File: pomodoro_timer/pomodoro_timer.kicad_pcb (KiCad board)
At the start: 2 copper layers, 68.1 x 78.1 mm, 37 parts, among them J1 UPDI Flash Header, J2 I2C Header, P1 Conn_USB_A_Plain, Q1 MOSFET SOT23, SW1 Start/Stop, SW2 Skip, SW3 Restart, U1 ATtiny412, U10 WS2812B, U11 WS2812B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

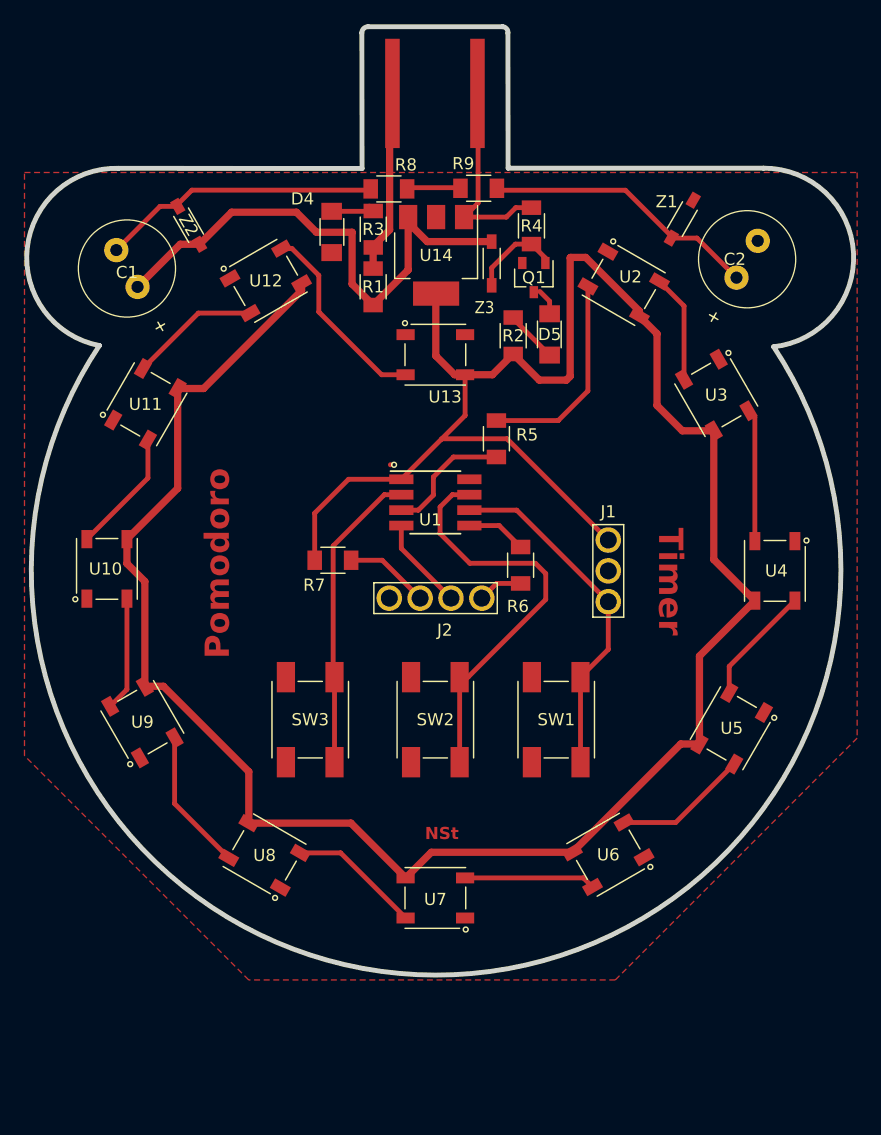
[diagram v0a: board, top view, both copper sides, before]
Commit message: PCB: updated schematics and routing
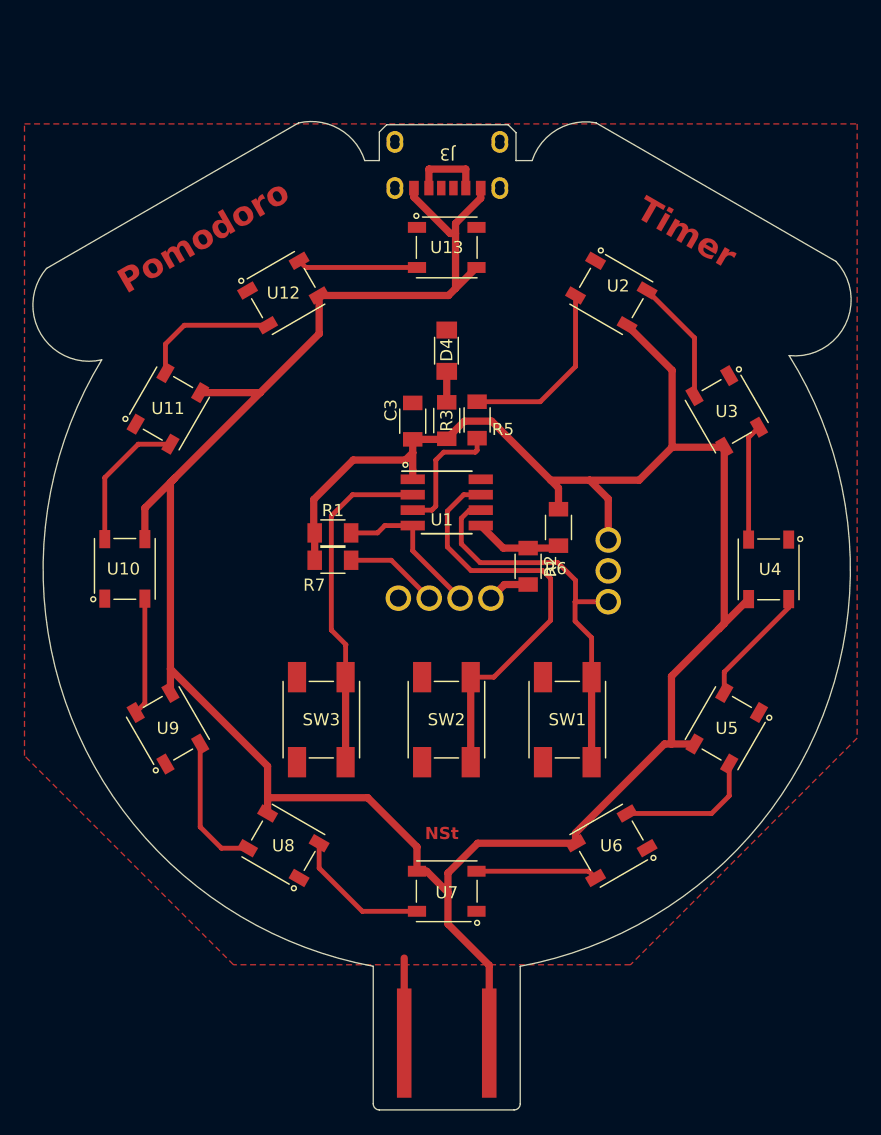
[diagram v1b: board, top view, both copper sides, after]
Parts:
- removed C1, C2: CP 10F, fab:CP_Elec_10F_Tecate_TPLC-3R8
- removed D5: Full LED, fab:LED_1206
- removed Q1: MOSFET SOT23, fab:SOT-23-3
- removed R4: 10K R, fab:R_1206
- removed R8, R9: 0R, fab:R_1206
- removed U14: Lin Reg 3.3V 1A, fab:SOT-223-3_TabPin2
- removed Z1, Z2: Diode 2.7V, fab:SOD-123
- removed Z3: Diode 4.9V, fab:SOD-123
- added C3: 100nF, fab:C_1206, F.Cu at (94.9, 106.8)
- added J3: Conn_USB_C_Socket_PowerOnly, fab:Conn_USB_C_Socket_GCT_USB4125-GF-A-0190, F.Cu at (97.8, 87.6)
- D4: value Charging LED -> Power LED
- J1, J2: moved to B.Cu
- R1: value 5.7R -> 1kR
- R2: value 100R -> 0R
- R6: value 0R -> 1kR
- moved P1 78.2 mm to (97.7, 158.0), turned to -90 degrees
- moved R1 20.5 mm to (88.3, 116.0), turned to 0 degrees
- moved R2 19.0 mm to (104.4, 118.8)
- moved R3 16.9 mm to (97.7, 106.8)
- moved D4 13.6 mm to (97.7, 101.0), turned to -90 degrees
- moved U13 8.88 mm to (97.7, 92.5)
- moved R6 4.41 mm to (106.9, 115.5)
- moved R5 2.22 mm to (100.2, 106.7)
- moved U9 2.17 mm to (74.8, 132.1)
- moved U11 1.88 mm to (74.8, 105.8)
- moved U12 1.76 mm to (84.2, 96.2)
- moved U8 1.74 mm to (84.2, 141.8)
- moved U3 1.60 mm to (120.8, 106.0)
- moved U10 1.48 mm to (71.2, 119.0)
- moved U2 1.26 mm to (111.2, 96.2)
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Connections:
- J1 pad 1: PWR_3V3 -> PWR_5V
- P1 pad 1: Net-(P1-5V) -> PWR_5V
- R1 pad 1: Net-(P1-5V) -> PWR_5V
- R1 pad 2: /5V -> SDA
- R2 pad 1: Net-(D5-A) -> SLC
- R2 pad 2: PWR_3V3 -> Net-(J2-Pin_1)
- R3 pad 2: Net-(P1-5V) -> PWR_5V
- R6 pad 1: SLC -> PWR_5V
- R6 pad 2: Net-(J2-Pin_1) -> SLC
- R7 pad 1: PWR_3V3 -> PWR_5V
- U1 pad 1: PWR_3V3 -> PWR_5V
- U10 pad 1: PWR_3V3 -> PWR_5V
- U11 pad 1: PWR_3V3 -> PWR_5V
- U12 pad 1: PWR_3V3 -> PWR_5V
- U13 pad 1: PWR_3V3 -> PWR_5V
- U2 pad 1: PWR_3V3 -> PWR_5V
- U3 pad 1: PWR_3V3 -> PWR_5V
- U4 pad 1: PWR_3V3 -> PWR_5V
- U5 pad 1: PWR_3V3 -> PWR_5V
- U6 pad 1: PWR_3V3 -> PWR_5V
- U7 pad 1: PWR_3V3 -> PWR_5V
- U8 pad 1: PWR_3V3 -> PWR_5V
- U9 pad 1: PWR_3V3 -> PWR_5V
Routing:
- net PWR_5V: track 0.00 -> 249.1 mm
- net PWR_3V3: track 219.5 -> 0.00 mm
- net Net-(Z1-K): track 50.5 -> 0.00 mm
- net /5V: track 44.0 -> 0.00 mm
- net Net-(P1-5V): track 13.2 -> 0.00 mm
- net /Mosfet 5V: track 7.55 -> 0.00 mm
- net Net-(U12-DOUT): track 16.3 -> 9.93 mm
- net SDA: track 7.67 -> 13.0 mm
- net Net-(D5-A): track 4.33 -> 0.00 mm
- net IN1: track 28.7 -> 32.9 mm
- net IN3: track 25.2 -> 28.2 mm
- net SLC: track 4.95 -> 7.25 mm
- net /Mosfet LED: track 2.18 -> 0.00 mm
- net Net-(U2-DIN): track 17.1 -> 15.1 mm
- net PWR_GND: track 14.7 -> 13.2 mm
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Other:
- board size 68.1 x 78.1 mm -> 67.4 x 81.4 mm
